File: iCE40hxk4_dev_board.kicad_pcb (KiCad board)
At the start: 2 copper layers, 114 parts, among them J1 USB_OTG, J201 CONN_01X02, J401 CONN_01X35, J501 CONN_01X35, U201 MIC2005A-2, U202 74xx125, U203 93LCxxB_sot-23-6, U204 MIC5355/6-xYMME, U205 FT2232H, U301 iCE40-HX4K-TQ144, U302 25LC_EEPROM, U501 AS4C1M16S

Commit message: Fist approach of board placement
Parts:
- removed J1: USB_OTG, Connectors:USB_Micro-B
- removed L1: BK0603HS330-T, Inductors_SMD:L_0603_HandSoldering
- added D202: LED_ALT, LEDs:LED_0603, F.Cu at (147.9, 151.8)
- added D203: RED, LEDs:LED_0603, F.Cu at (152.2, 150.0)
- added D204: GREEN, LEDs:LED_0603, F.Cu at (152.0, 151.8)
- added D205: GREEN, LEDs:LED_0603, F.Cu at (187.7, 124.3)
- added D206: YELLOW, LEDs:LED_0603, F.Cu at (187.7, 122.8)
- added D207: RED, LEDs:LED_0603, F.Cu at (187.7, 121.3)
- added D401: GREEN, LEDs:LED_0603, F.Cu at (258.4, 22.4)
- added D402: GREEN, LEDs:LED_0603, F.Cu at (253.7, 22.4)
- added D403: GREEN, LEDs:LED_0603, F.Cu at (183.2, 22.4)
- added D404: GREEN, LEDs:LED_0603, F.Cu at (220.8, 22.4)
- added D405: GREEN, LEDs:LED_0603, F.Cu at (211.4, 22.4)
- added D406: GREEN, LEDs:LED_0603, F.Cu at (202.0, 22.4)
- added D407: GREEN, LEDs:LED_0603, F.Cu at (263.1, 22.4)
- added D408: GREEN, LEDs:LED_0603, F.Cu at (239.6, 22.4)
- added J202: USB_OTG, Connectors:USB_Micro-B, F.Cu at (158.8, 166.5)
- added L202: BK0603HS330-T, Inductors_SMD:L_0603_HandSoldering, F.Cu at (156.2, 160.6)
- added R229: 0, Resistors_SMD:R_0603_HandSoldering, F.Cu at (168.1, 112.3)
- added R230: 0, Resistors_SMD:R_0603_HandSoldering, F.Cu at (166.7, 112.3)
- added R231: 0, Resistors_SMD:R_0603_HandSoldering, F.Cu at (165.3, 112.3)
- added R232: 680, Resistors_SMD:R_0603_HandSoldering, F.Cu at (191.7, 124.2)
- added R233: 680, Resistors_SMD:R_0603_HandSoldering, F.Cu at (191.6, 122.8)
- added R234: 680, Resistors_SMD:R_0603_HandSoldering, F.Cu at (191.6, 121.2)
- added R401: 680, Resistors_SMD:R_0603_HandSoldering, F.Cu at (159.7, 22.2)
- added R402: 680, Resistors_SMD:R_0603_HandSoldering, F.Cu at (56.2, 22.2)
- added R403: 680, Resistors_SMD:R_0603_HandSoldering, F.Cu at (169.1, 22.2)
- added R404: 680, Resistors_SMD:R_0603_HandSoldering, F.Cu at (65.6, 22.2)
- added R405: 680, Resistors_SMD:R_0603_HandSoldering, F.Cu at (98.5, 22.2)
- added R406: 680, Resistors_SMD:R_0603_HandSoldering, F.Cu at (108.0, 22.2)
- added R407: 680, Resistors_SMD:R_0603_HandSoldering, F.Cu at (241.0, 183.2)
- added R408: 680, Resistors_SMD:R_0603_HandSoldering, F.Cu at (225.5, 22.2)
- R202: value 0 -> 1500; footprint Resistors_SMD:R_1206_HandSoldering -> Resistors_SMD:R_0603_HandSoldering
- R204: value 10k -> 1500
- R205: value 2k2 -> 1500
- R206: value 10k -> 0; footprint Resistors_SMD:R_0603_HandSoldering -> Resistors_SMD:R_1206_HandSoldering
- R208: value 12k -> 2k2
- R209: value 1k -> 10k
- R210: value 0 -> 10k
- R211: value 0 -> 12k
- R212: value 0 -> 1k
- U204: footprint TO_SOT_Packages_SMD:SOT-23-6 -> TO_SOT_Packages_SMD:SOT-23-8_Handsoldering
- moved J501 229.2 mm to (325.0, 83.3)
- moved C501 153.0 mm to (277.2, 22.3)
- moved C503 150.1 mm to (23.3, 22.3)
- moved C510 149.1 mm to (272.5, 22.3)
- moved C508 145.2 mm to (267.8, 22.3)
- moved R305 142.3 mm to (32.7, 22.2)
- moved R307 138.6 mm to (37.4, 22.2)
- moved C223 133.2 mm to (101.4, 183.2)
- moved R308 131.1 mm to (46.8, 22.2)
- moved C218 127.9 mm to (91.8, 183.2)
- moved R209 127.5 mm to (51.5, 22.2)
- moved R212 120.5 mm to (60.9, 22.2)
- moved C215 118.8 mm to (80.3, 140.4)
- moved C502 115.9 mm to (257.2, 145.1)
- moved C507 108.8 mm to (252.4, 137.5)
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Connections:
- R202 pad 1: Net-(R202-Pad1) -> /USB+OSCILLATOR+REGULATOR/Vext_filtered
- R202 pad 2: GND -> Net-(D202-Pad2)
- R203 pad 1: +3V3 -> Net-(R203-Pad1)
- R203 pad 2: Net-(R202-Pad1) -> GND
- R204 pad 1: +3V3 -> Net-(D204-Pad2)
- R204 pad 2: /USB+OSCILLATOR+REGULATOR/EECS -> /USB+OSCILLATOR+REGULATOR/Vbus_filtered
- R205 pad 1: /USB+OSCILLATOR+REGULATOR/EEDATA -> Net-(D203-Pad2)
- R206 pad 2: /USB+OSCILLATOR+REGULATOR/EECLK -> Net-(R203-Pad1)
- R207 pad 2: /USB+OSCILLATOR+REGULATOR/EEDATA -> /USB+OSCILLATOR+REGULATOR/EECS
- R208 pad 1: Net-(R208-Pad1) -> /USB+OSCILLATOR+REGULATOR/EEDATA
- R208 pad 2: GND -> Net-(R208-Pad2)
- R209 pad 1: Net-(R209-Pad1) -> +3V3
- R209 pad 2: +3V3 -> /USB+OSCILLATOR+REGULATOR/EECLK
- R210 pad 1: /FPGA_PROGRAMMING+POWER/SCK -> +3V3
- R210 pad 2: Net-(R210-Pad2) -> /USB+OSCILLATOR+REGULATOR/EEDATA
- R211 pad 1: /FPGA_PROGRAMMING+POWER/MOSI -> Net-(R211-Pad1)
- R211 pad 2: Net-(R211-Pad2) -> GND
- R212 pad 1: /FPGA_PROGRAMMING+POWER/MISO -> Net-(R212-Pad1)
- R212 pad 2: Net-(R212-Pad2) -> +3V3
- R213 pad 1: /FPGA_PROGRAMMING+POWER/SS -> /FPGA_PROGRAMMING+POWER/SCK
- R214 pad 1: /FPGA_PROGRAMMING+POWER/CDONE -> /FPGA_PROGRAMMING+POWER/MOSI
- R215 pad 1: /FPGA_PROGRAMMING+POWER/CRESET -> /FPGA_PROGRAMMING+POWER/MISO
- R216 pad 1: /RAM+LEFT_BOTTOM_BANKs/D0 -> /FPGA_PROGRAMMING+POWER/SS
- R217 pad 1: /RAM+LEFT_BOTTOM_BANKs/D1 -> /FPGA_PROGRAMMING+POWER/CDONE
- R218 pad 1: /RAM+LEFT_BOTTOM_BANKs/D2 -> /FPGA_PROGRAMMING+POWER/CRESET
- R219 pad 1: /RAM+LEFT_BOTTOM_BANKs/D3 -> /RAM+LEFT_BOTTOM_BANKs/D0
- R220 pad 1: /RAM+LEFT_BOTTOM_BANKs/D4 -> /RAM+LEFT_BOTTOM_BANKs/D1
- R221 pad 1: /RAM+LEFT_BOTTOM_BANKs/D5 -> /RAM+LEFT_BOTTOM_BANKs/D2
- R222 pad 1: /RAM+LEFT_BOTTOM_BANKs/D6 -> /RAM+LEFT_BOTTOM_BANKs/D3
- R223 pad 1: /RAM+LEFT_BOTTOM_BANKs/D7 -> /RAM+LEFT_BOTTOM_BANKs/D4
- R224 pad 1: /RAM+LEFT_BOTTOM_BANKs/~RXF -> /RAM+LEFT_BOTTOM_BANKs/D5
- R225 pad 1: /RAM+LEFT_BOTTOM_BANKs/~TXE -> /RAM+LEFT_BOTTOM_BANKs/D6
- R226 pad 1: /RAM+LEFT_BOTTOM_BANKs/~RD -> /RAM+LEFT_BOTTOM_BANKs/D7
- R227 pad 1: /RAM+LEFT_BOTTOM_BANKs/~WR -> /RAM+LEFT_BOTTOM_BANKs/~RXF
- R228 pad 1: /RAM+LEFT_BOTTOM_BANKs/SIWU -> /RAM+LEFT_BOTTOM_BANKs/~TXE
- U201 pad 4: Net-(U201-Pad4) -> Net-(R205-Pad2)
- U202 pad 10: Net-(R202-Pad1) -> Net-(R203-Pad1)
- U202 pad 11: Net-(U202-Pad11) -> (no net)
- U202 pad 8: /USB+OSCILLATOR+REGULATOR/OSC2 -> (no net)
- U203 pad 1: Net-(R205-Pad2) -> Net-(R208-Pad2)
- U205 pad 14: Net-(R209-Pad1) -> Net-(R212-Pad1)
- U205 pad 16: Net-(R210-Pad2) -> Net-(R213-Pad2)
- U205 pad 17: Net-(R211-Pad2) -> Net-(R214-Pad2)
- U205 pad 18: Net-(R212-Pad2) -> Net-(R215-Pad2)
- U205 pad 19: Net-(U205-Pad19) -> (no net)
- U205 pad 21: Net-(R213-Pad2) -> Net-(R216-Pad2)
- U205 pad 22: Net-(U205-Pad22) -> (no net)
- U205 pad 23: Net-(R214-Pad2) -> Net-(R217-Pad2)
- U205 pad 24: Net-(R215-Pad2) -> Net-(R218-Pad2)
- U205 pad 29: Net-(U205-Pad29) -> (no net)
- U205 pad 3: Net-(U205-Pad3) -> (no net)
- U205 pad 30: Net-(U205-Pad30) -> (no net)
- U205 pad 32: Net-(U205-Pad32) -> (no net)
- U205 pad 33: Net-(U205-Pad33) -> (no net)
- U205 pad 34: Net-(U205-Pad34) -> (no net)
- U205 pad 36: Net-(U205-Pad36) -> (no net)
- U205 pad 38: Net-(R216-Pad2) -> Net-(R219-Pad2)
- U205 pad 39: Net-(R217-Pad2) -> Net-(R220-Pad2)
- U205 pad 40: Net-(R218-Pad2) -> Net-(R221-Pad2)
- U205 pad 41: Net-(R219-Pad2) -> Net-(R222-Pad2)
- U205 pad 43: Net-(R220-Pad2) -> Net-(R223-Pad2)
- U205 pad 44: Net-(R221-Pad2) -> Net-(R224-Pad2)
- U205 pad 45: Net-(R222-Pad2) -> Net-(R225-Pad2)
- U205 pad 46: Net-(R223-Pad2) -> Net-(R226-Pad2)
- U205 pad 48: Net-(R224-Pad2) -> Net-(R227-Pad2)
- U205 pad 52: Net-(R225-Pad2) -> Net-(R228-Pad2)
- U205 pad 53: Net-(R226-Pad2) -> Net-(R229-Pad2)
- U205 pad 54: Net-(R227-Pad2) -> Net-(R230-Pad2)
- U205 pad 55: Net-(R228-Pad2) -> Net-(R231-Pad2)
- U205 pad 57: Net-(U205-Pad57) -> (no net)
- U205 pad 58: Net-(U205-Pad58) -> (no net)
- U205 pad 59: Net-(U205-Pad59) -> (no net)
- U205 pad 6: Net-(R208-Pad1) -> Net-(R211-Pad1)
- U205 pad 60: Net-(U205-Pad60) -> (no net)
- U301 pad 109: Net-(U301-Pad109) -> (no net)
- U301 pad 118: /RIGHT_TOP_BANKs/ADC_0 -> (no net)
- U301 pad 119: /RIGHT_TOP_BANKs/ADC_1 -> (no net)
- U301 pad 120: /RIGHT_TOP_BANKs/ADC_2 -> (no net)
- U301 pad 121: /RIGHT_TOP_BANKs/ADC_3 -> (no net)
- U301 pad 122: /RIGHT_TOP_BANKs/ADC_4 -> (no net)
- U301 pad 124: /RIGHT_TOP_BANKs/ADC_5 -> (no net)
- U301 pad 125: /RIGHT_TOP_BANKs/ADC_6 -> (no net)
- U301 pad 128: /RIGHT_TOP_BANKs/ADC_7 -> (no net)
- U301 pad 129: /RIGHT_TOP_BANKs/ADC_8 -> (no net)
- U301 pad 130: /RIGHT_TOP_BANKs/ADC_9 -> (no net)
- U301 pad 133: Net-(U301-Pad133) -> (no net)
- U301 pad 134: /RIGHT_TOP_BANKs/ADC_10 -> (no net)
- U301 pad 135: /RIGHT_TOP_BANKs/ADC_11 -> (no net)
- U301 pad 136: /RIGHT_TOP_BANKs/ADC_12 -> (no net)
- U301 pad 137: /RIGHT_TOP_BANKs/ADC_13 -> (no net)
- U301 pad 138: /RIGHT_TOP_BANKs/ADC_14 -> (no net)
- U301 pad 139: /RIGHT_TOP_BANKs/ADC_15 -> (no net)
- U301 pad 141: /RIGHT_TOP_BANKs/ADC_16 -> (no net)
- U301 pad 142: /RIGHT_TOP_BANKs/ADC_17 -> (no net)
- U301 pad 35: Net-(U301-Pad35) -> (no net)
- U301 pad 36: Net-(U301-Pad36) -> (no net)
- U301 pad 50: Net-(U301-Pad50) -> (no net)
- U301 pad 51: Net-(U301-Pad51) -> (no net)
- U301 pad 58: Net-(U301-Pad58) -> (no net)
- U301 pad 77: Net-(U301-Pad77) -> (no net)
- U501 pad 33: Net-(U501-Pad33) -> (no net)
- U501 pad 37: Net-(U501-Pad37) -> (no net)
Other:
- copper layers 2 -> 4

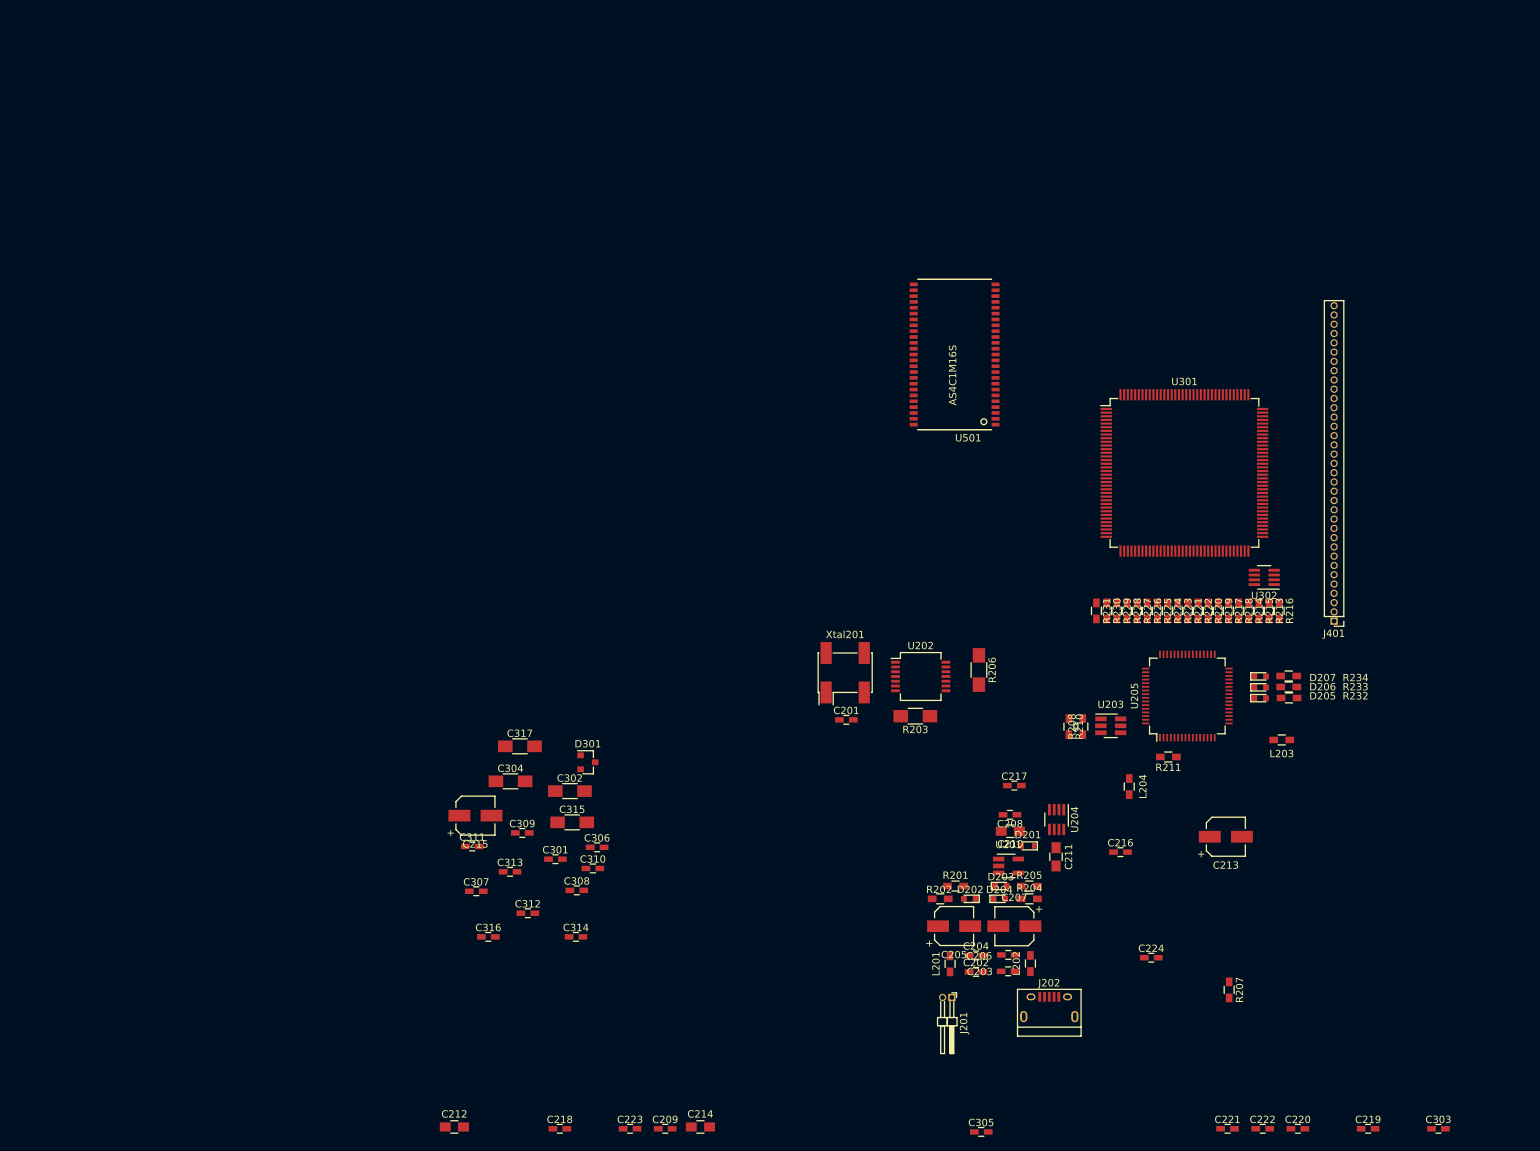
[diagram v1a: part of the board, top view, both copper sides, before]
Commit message: Clk's buffers were removed and pcb routing was started
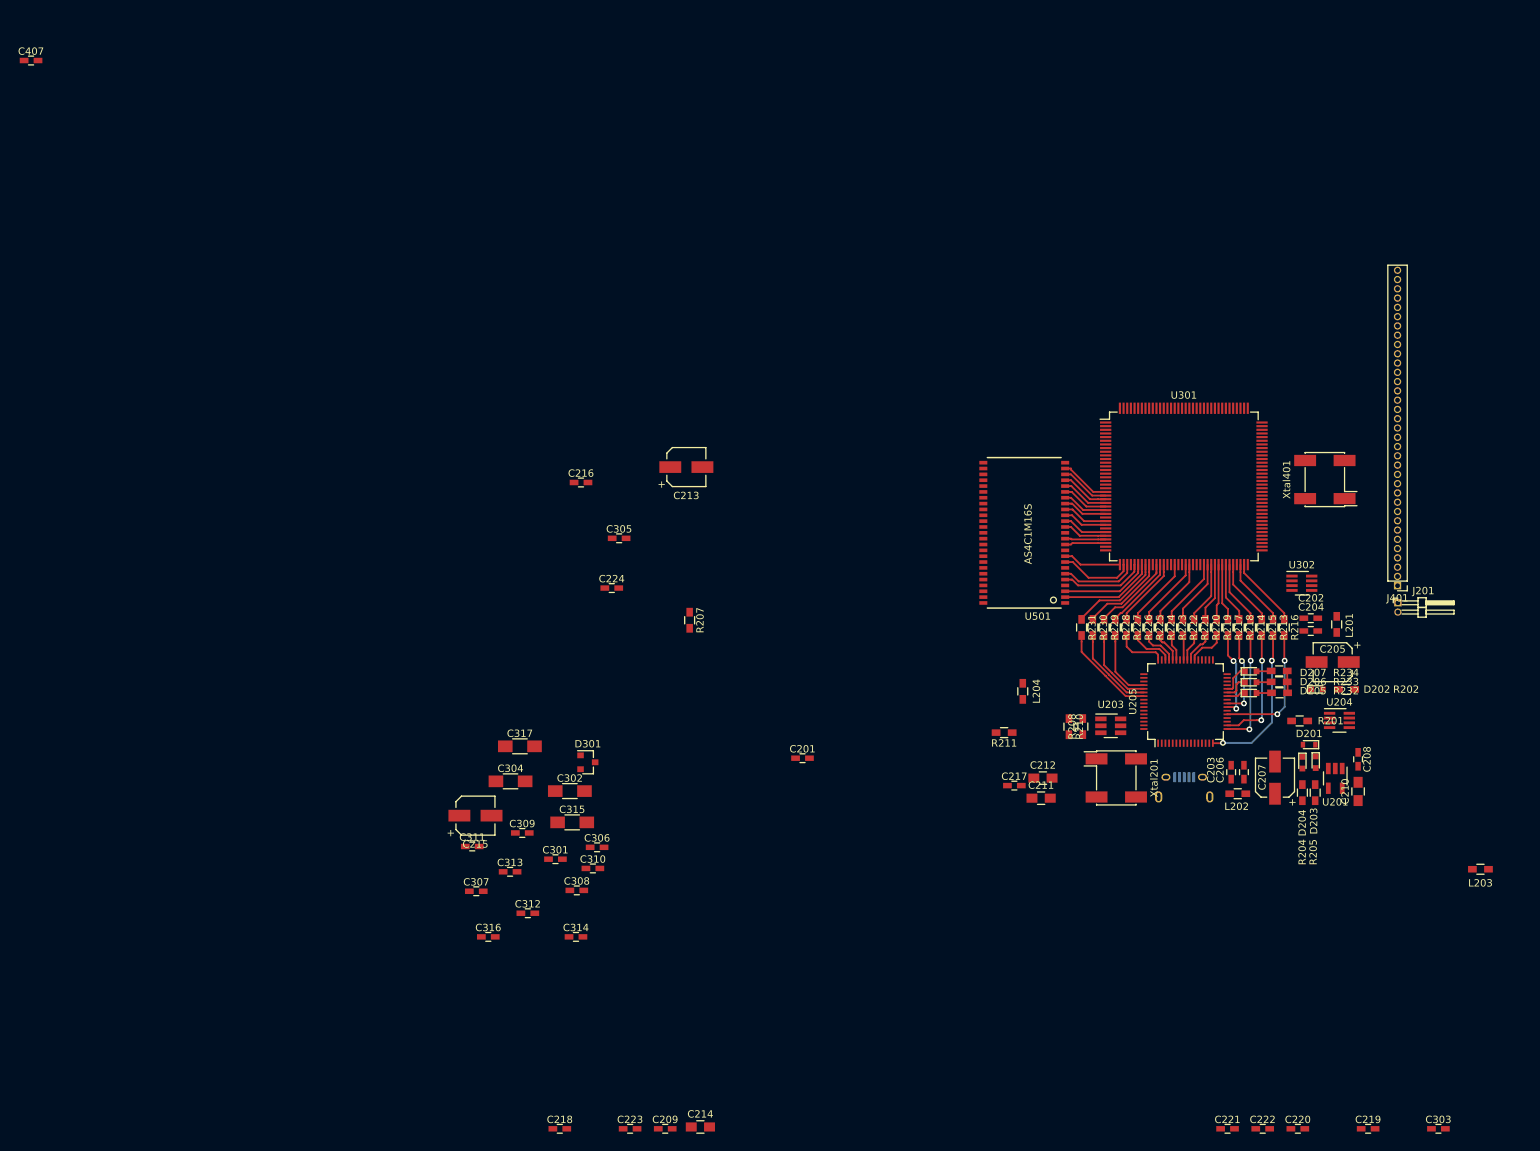
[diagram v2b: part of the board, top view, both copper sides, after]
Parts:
- removed R203, R206: 0, Resistors_SMD:R_1206_HandSoldering
- removed U202: 74xx125, Housings_SSOP:SSOP-14_5.3x6.2mm_Pitch0.65mm
- added C407: 100nF, Capacitors_SMD:C_0603_HandSoldering, F.Cu at (19.4, 37.0)
- added Xtal401: LFSPXO019966, Oscillators:Oscillator_SMD_Fordahl_DFAS11-4pin_7.0x5.0mm_HandSoldering, F.Cu at (196.6, 94.4)
- J202: moved to B.Cu
- moved C305 95.2 mm to (100.0, 102.4)
- moved C212 93.7 mm to (158.0, 135.2)
- moved C216 89.5 mm to (94.7, 94.8)
- moved R207 89.5 mm to (109.6, 113.6)
- moved C224 89.5 mm to (98.9, 109.2)
- moved C213 89.5 mm to (109.2, 92.7)
- moved J201 81.5 mm to (206.6, 111.2), turned to 0 degrees
- moved L201 70.4 mm to (198.2, 114.2), turned to 270 degrees
- moved C202 66.7 mm to (194.6, 113.3), turned to 180 degrees
- moved C204 63.8 mm to (194.6, 115.1), turned to 180 degrees
- moved C205 63.2 mm to (197.6, 119.3), turned to 180 degrees
- moved R202 62.6 mm to (199.5, 123.1), turned to 180 degrees
- moved D202 55.5 mm to (195.5, 123.1), turned to 0 degrees
- moved R201 52.2 mm to (193.1, 127.4), turned to 180 degrees
- moved C208 48.3 mm to (201.1, 132.7), turned to 270 degrees
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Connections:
- U205 pad 2: Net-(U202-Pad3) -> Net-(U205-Pad2)
- U301 pad 94: /USB+OSCILLATOR+REGULATOR/OSC1 -> /RIGHT_TOP_BANKs/OSC
- Xtal201 pad 3: Net-(U202-Pad2) -> Net-(U205-Pad2)
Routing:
- net Net-(R213-Pad2): track 0.00 -> 21.2 mm, vias 0 -> 2
- net Net-(R216-Pad2): track 0.00 -> 18.1 mm, vias 0 -> 2
- net Net-(R215-Pad2): track 0.00 -> 16.6 mm, vias 0 -> 2
- net Net-(R214-Pad2): track 0.00 -> 16.0 mm, vias 0 -> 2
- net Net-(R231-Pad2): track 0.00 -> 13.3 mm
- net /RAM+LEFT_BOTTOM_BANKs/DQ0: track 0.00 -> 13.1 mm
- net /RAM+LEFT_BOTTOM_BANKs/SIWU: track 0.00 -> 12.8 mm
- net /RAM+LEFT_BOTTOM_BANKs/DQ1: track 0.00 -> 12.2 mm
- net Net-(R230-Pad2): track 0.00 -> 12.1 mm
- net Net-(R218-Pad2): track 0.00 -> 11.9 mm, vias 0 -> 2
- net Net-(R217-Pad2): track 0.00 -> 11.8 mm, vias 0 -> 2
- net /RAM+LEFT_BOTTOM_BANKs/~WR: track 0.00 -> 11.8 mm
- net /RAM+LEFT_BOTTOM_BANKs/DQ2: track 0.00 -> 11.6 mm
- net /RAM+LEFT_BOTTOM_BANKs/~RD: track 0.00 -> 11.1 mm
- net Net-(R229-Pad2): track 0.00 -> 10.9 mm
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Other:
- net class Default: via_dia 0.6 -> 0.8
- rule trace_min: 0.2 -> 0.15
- rule via_min_drill: 0.3 -> 0.4
- rule via_min_size: 0.4 -> 0.7

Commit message: Placing de algunos capas de acople y otras giladas
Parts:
- C201, C209, C214, C215, C216, C217, C302, C303, C305, C307, C309, C311, C312, C314, L204, R303: moved to B.Cu
- C213: footprint Capacitors_SMD:CP_Elec_5x5.7 -> Capacitors_SMD:C_1206_HandSoldering; moved to B.Cu
- moved R305 188.7 mm to (199.5, 110.4), turned to 180 degrees
- moved R212 163.0 mm to (181.4, 132.0)
- moved R209 153.1 mm to (165.8, 124.1)
- moved C307 122.0 mm to (185.0, 88.1), turned to 270 degrees
- moved J501 104.6 mm to (221.0, 72.4)
- moved C215 102.6 mm to (182.2, 128.1)
- moved C312 102.1 mm to (174.6, 100.7), turned to 90 degrees
- moved C311 100.0 mm to (170.9, 103.3)
- moved R304 98.1 mm to (198.6, 107.6)
- moved C314 97.8 mm to (176.7, 104.8), turned to 180 degrees
- moved C309 93.6 mm to (169.3, 98.6), turned to 90 degrees
- moved C302 92.3 mm to (177.5, 99.6), turned to 90 degrees
- moved C303 90.2 mm to (175.8, 100.7), turned to 90 degrees
- moved C214 88.1 mm to (174.9, 122.2)
- moved C216 87.9 mm to (176.1, 127.8)
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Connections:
- J202 pad 4: (no net) -> Net-(J202-Pad4)
- U205 pad 19: (no net) -> Net-(U205-Pad19)
- U205 pad 22: (no net) -> Net-(U205-Pad22)
- U205 pad 29: (no net) -> Net-(U205-Pad29)
- U205 pad 3: (no net) -> Net-(U205-Pad3)
- U205 pad 30: (no net) -> Net-(U205-Pad30)
- U205 pad 32: (no net) -> Net-(U205-Pad32)
- U205 pad 33: (no net) -> Net-(U205-Pad33)
- U205 pad 34: (no net) -> Net-(U205-Pad34)
- U205 pad 36: (no net) -> Net-(U205-Pad36)
- U205 pad 57: (no net) -> Net-(U205-Pad57)
- U205 pad 58: (no net) -> Net-(U205-Pad58)
- U205 pad 59: (no net) -> Net-(U205-Pad59)
- U205 pad 60: (no net) -> Net-(U205-Pad60)
- U301 pad 109: (no net) -> Net-(U301-Pad109)
- U301 pad 118: (no net) -> /RIGHT_TOP_BANKs/ADC_0
- U301 pad 119: (no net) -> /RIGHT_TOP_BANKs/ADC_1
- U301 pad 120: (no net) -> /RIGHT_TOP_BANKs/ADC_2
- U301 pad 121: (no net) -> /RIGHT_TOP_BANKs/ADC_3
- U301 pad 122: (no net) -> /RIGHT_TOP_BANKs/ADC_4
- U301 pad 124: (no net) -> /RIGHT_TOP_BANKs/ADC_5
- U301 pad 125: (no net) -> /RIGHT_TOP_BANKs/ADC_6
- U301 pad 128: (no net) -> /RIGHT_TOP_BANKs/ADC_7
- U301 pad 129: (no net) -> /RIGHT_TOP_BANKs/ADC_8
- U301 pad 130: (no net) -> /RIGHT_TOP_BANKs/ADC_9
- U301 pad 133: (no net) -> Net-(U301-Pad133)
- U301 pad 134: (no net) -> /RIGHT_TOP_BANKs/ADC_10
- U301 pad 135: (no net) -> /RIGHT_TOP_BANKs/ADC_11
- U301 pad 136: (no net) -> /RIGHT_TOP_BANKs/ADC_12
- U301 pad 137: (no net) -> /RIGHT_TOP_BANKs/ADC_13
- U301 pad 138: (no net) -> /RIGHT_TOP_BANKs/ADC_14
- U301 pad 139: (no net) -> /RIGHT_TOP_BANKs/ADC_15
- U301 pad 141: (no net) -> /RIGHT_TOP_BANKs/ADC_16
- U301 pad 142: (no net) -> /RIGHT_TOP_BANKs/ADC_17
- U301 pad 35: (no net) -> Net-(U301-Pad35)
- U301 pad 36: (no net) -> Net-(U301-Pad36)
- U301 pad 50: (no net) -> Net-(U301-Pad50)
- U301 pad 51: (no net) -> Net-(U301-Pad51)
- U301 pad 58: (no net) -> Net-(U301-Pad58)
- U301 pad 77: (no net) -> Net-(U301-Pad77)
- U501 pad 33: (no net) -> Net-(U501-Pad33)
- U501 pad 37: (no net) -> Net-(U501-Pad37)
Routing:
- net /FPGA_PROGRAMMING+POWER/+1.2V: track 0.00 -> 64.1 mm, vias 0 -> 10
- net GND: track 0.00 -> 30.6 mm, vias 0 -> 19
- net +3V3: track 3.02 -> 25.5 mm, vias 0 -> 5
- net /USB+OSCILLATOR+REGULATOR/EEDATA: track 0.00 -> 16.4 mm
- net Net-(C213-Pad1): track 0.00 -> 14.2 mm, vias 0 -> 2
- net Net-(R304-Pad2): track 0.00 -> 13.8 mm, vias 0 -> 2
- net /USB+OSCILLATOR+REGULATOR/EECLK: track 0.00 -> 13.3 mm
- net /FPGA_PROGRAMMING+POWER/SCK: track 9.35 -> 22.5 mm, vias 0 -> 2
- net /FPGA_PROGRAMMING+POWER/MOSI: track 8.69 -> 20.3 mm, vias 0 -> 2
- net /FPGA_PROGRAMMING+POWER/MISO: track 9.12 -> 17.5 mm, vias 0 -> 2
- net /USB+OSCILLATOR+REGULATOR/EECS: track 0.00 -> 7.78 mm
- net /FPGA_PROGRAMMING+POWER/SS: track 9.78 -> 16.6 mm
- net Net-(U205-Pad2): track 0.00 -> 5.61 mm
- net Net-(R305-Pad2): track 0.00 -> 4.64 mm
- net Net-(C215-Pad1): track 0.00 -> 4.56 mm, vias 0 -> 2
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- added copper zone on F.Cu, net +3V3
